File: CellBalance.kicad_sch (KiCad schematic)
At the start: 9 parts

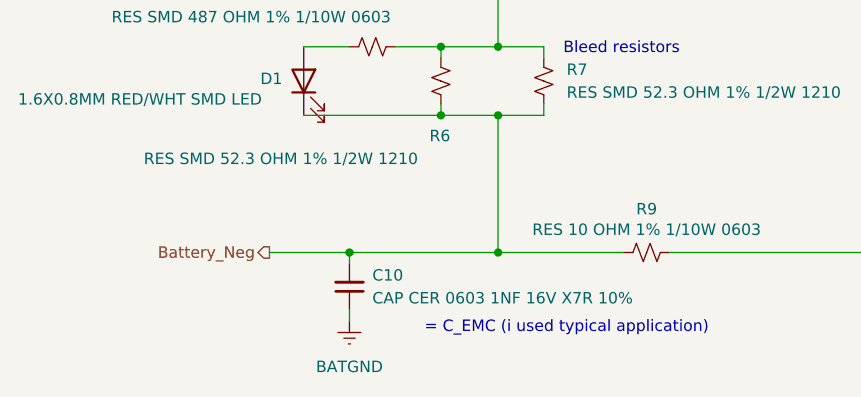
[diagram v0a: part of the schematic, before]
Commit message: fixed capacitor values
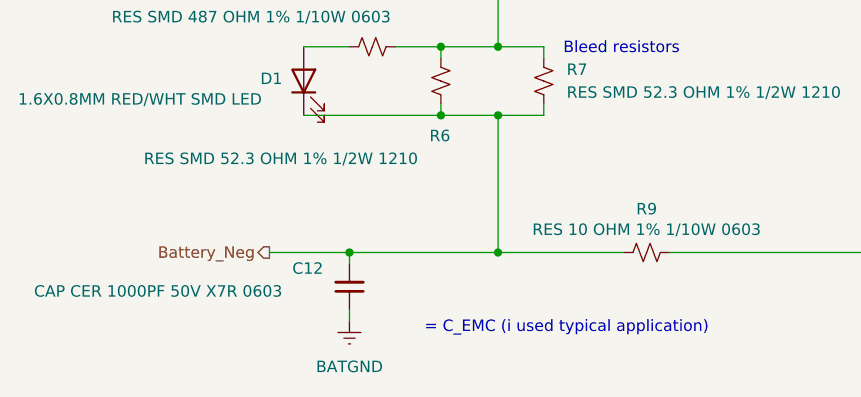
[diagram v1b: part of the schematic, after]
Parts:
- removed C10: CAP CER 0603 1NF 16V X7R 10%, Capacitor_SMD:C_0603_1608Metric, symbol Device:C_Small
- added C12: CAP CER 1000PF 50V X7R 0603, Capacitor_SMD:C_0603_1608Metric, symbol Device:C_Small
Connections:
- net BATGND: now also C12.1
- net Battery_Neg: now also C12.2
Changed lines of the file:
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@@
-	)
-	(symbol
-		(lib_id "Device:C_Small")
-		(at 119.38 123.19 180)
-		(unit 1)
-		(body_style 1)
-		(exclude_from_sim no)
-		(in_bom yes)
-		(on_board yes)
-		(in_pos_files yes)
-		(dnp no)
-		(fields_autoplaced yes)
-		(property "Reference" "C10"
-			(at 121.92 121.9135 0)
-			(show_name no)
-			(do_not_autoplace no)
-			(effects
-				(font
-					(size 1.27 1.27)
-				)
-				(justify right)
-			)
-		)
-		(property "Value" "CAP CER 0603 1NF 16V X7R 10%"
-			(at 121.92 124.4535 0)
-			(show_name no)
-			(do_not_autoplace no)
-			(effects
-				(font
-					(size 1.27 1.27)
-				)
-				(justify right)
-			)
-		)
-		(property "Footprint" "Capacitor_SMD:C_0603_1608Metric"
-			(at 119.38 123.19 0)
-			(hide yes)
-			(show_name no)
-			(do_not_autoplace no)
-			(effects
-				(font
-					(size 1.27 1.27)
-				)
-			)
-		)
-		(property "Datasheet" "https://www.digikey.ca/en/products/detail/kemet/C0603C102K4RECAUTO/8640472"
-			(at 119.38 123.19 0)
-			(hide yes)
-			(show_name no)
-			(do_not_autoplace no)
-			(effects
-				(font
-					(size 1.27 1.27)
-				)
-			)
-		)
-		(property "Description" "1000 pF ±10% 16V Ceramic Capacitor X7R 0603 (1608 Metric)"
-			(at 119.38 123.19 0)
-			(hide yes)
-			(show_name no)
-			(do_not_autoplace no)
-			(effects
-				(font
-					(size 1.27 1.27)
-				)
-			)
-		)
-		(pin "2"
-		)
-		(pin "1"
-		)
-		(instances
-			(project "bms-afe"
-				(path "/226a23e7-09bb-40bc-b53a-ec42a6b7cc90/199aea63-5bfb-41be-ba55-0a021bc0a074"
-					(reference "C34")
-					(unit 1)
-				)
-				(path "/226a23e7-09bb-40bc-b53a-ec42a6b7cc90/2aa084bd-01e7-47e5-8f6d-30b4f325d7f4"
-					(reference "C12")
-					(unit 1)
-				)
-				(path "/226a23e7-09bb-40bc-b53a-ec42a6b7cc90/30f9ba51-47e3-4adb-895f-80ddd8089ec1"
-					(reference "C38")
-					(unit 1)
-				)
-				(path "/226a23e7-09bb-40bc-b53a-ec42a6b7cc90/9ef805d4-1601-4480-b9fd-3e26be539576"
-					(reference "C40")
-					(unit 1)
-				)
-				(path "/226a23e7-09bb-40bc-b53a-ec42a6b7cc90/a6f93463-0553-4e94-825f-86704d73fcd7"
-					(reference "C10")
-					(unit 1)
-				)
-				(path "/226a23e7-09bb-40bc-b53a-ec42a6b7cc90/cf97efbe-7ee9-4abe-8844-0d879c082204"
-					(reference "C36")
-					(unit 1)
-				)
-			)
-		)
 	)
 	(symbol
@@
 					(unit 1)
 				)
+			)
+		)
+	)
+	(symbol
+		(lib_id "Device:C_Small")
+		(at 119.38 123.19 180)
+		(unit 1)
+		(body_style 1)
+		(exclude_from_sim no)
+		(in_bom yes)
+		(on_board yes)
+		(in_pos_files yes)
+		(dnp no)
+		(property "Reference" "C12"
+			(at 113.03 121.158 0)
+			(show_name no)
+			(do_not_autoplace no)
+			(effects
+				(font
+					(size 1.27 1.27)
+				)
+				(justify right)
+			)
+		)
+		(property "Value" "CAP CER 1000PF 50V X7R 0603"
+			(at 84.328 123.698 0)
+			(show_name no)
+			(do_not_autoplace no)
+			(effects
+				(font
+					(size 1.27 1.27)
+				)
+				(justify right)
+			)
+		)
+		(property "Footprint" "Capacitor_SMD:C_0603_1608Metric"
+			(at 119.38 123.19 0)
+			(hide yes)
+			(show_name no)
+			(do_not_autoplace no)
+			(effects
+				(font
+					(size 1.27 1.27)
+				)
+			)
+		)
+		(property "Datasheet" "https://www.digikey.ca/en/products/detail/samsung-electro-mechanics/CL10B102KB8NNNC/3886676"
+			(at 119.38 123.19 0)
+			(hide yes)
+			(show_name no)
+			(do_not_autoplace no)
+			(effects
+				(font
+					(size 1.27 1.27)
+				)
+			)
+		)
+		(property "Description" "1000 pF ±10% 50V Ceramic Capacitor X7R 0603 (1608 Metric)"
+			(at 119.38 123.19 0)
+			(hide yes)
+			(show_name no)
+			(do_not_autoplace no)
+			(effects
+				(font
+					(size 1.27 1.27)
+				)
+			)
+		)
+		(pin "2"
+		)
+		(pin "1"
+		)
+		(instances
+			(project "bms-afe"
+				(path "/226a23e7-09bb-40bc-b53a-ec42a6b7cc90/199aea63-5bfb-41be-ba55-0a021bc0a074"
+					(reference "C31")
+					(unit 1)
+				)
+				(path "/226a23e7-09bb-40bc-b53a-ec42a6b7cc90/2aa084bd-01e7-47e5-8f6d-30b4f325d7f4"
+					(reference "C26")
+					(unit 1)
+				)
+				(path "/226a23e7-09bb-40bc-b53a-ec42a6b7cc90/30f9ba51-47e3-4adb-895f-80ddd8089ec1"
+					(reference "C33")
+					(unit 1)
+				)
+				(path "/226a23e7-09bb-40bc-b53a-ec42a6b7cc90/9ef805d4-1601-4480-b9fd-3e26be539576"
+					(reference "C34")
+					(unit 1)
+				)
+				(path "/226a23e7-09bb-40bc-b53a-ec42a6b7cc90/a6f93463-0553-4e94-825f-86704d73fcd7"
+					(reference "C12")
+					(unit 1)
+				)
+				(path "/226a23e7-09bb-40bc-b53a-ec42a6b7cc90/cf97efbe-7ee9-4abe-8844-0d879c082204"
+					(reference "C32")
+					(unit 1)
+				)
